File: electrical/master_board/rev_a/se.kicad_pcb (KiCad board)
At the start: 2 copper layers, 0 parts

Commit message: Inject the PCB outlines into master/center/ne/nw/se/sw PCB's.
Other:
- board outline added: 64.7 x 45 mm
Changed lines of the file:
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@@
     (uvia_drill 0.1)
   )
+  (gr_line (start 107.50 158.60) (end 107.50 179.49) (layer Edge.Cuts) (width 0.05))
+  (gr_line (start 107.50 179.49) (end 107.51 179.62) (layer Edge.Cuts) (width 0.05))
+  (gr_line (start 107.51 179.62) (end 107.52 179.76) (layer Edge.Cuts) (width 0.05))
+  (gr_line (start 107.52 179.76) (end 107.55 179.89) (layer Edge.Cuts) (width 0.05))
+  (gr_line (start 107.55 179.89) (end 107.59 180.01) (layer Edge.Cuts) (width 0.05))
+  (gr_line (start 107.59 180.01) (end 107.64 180.14) (layer Edge.Cuts) (width 0.05))
+  (gr_line (start 107.64 180.14) (end 107.71 180.25) (layer Edge.Cuts) (width 0.05))
+  (gr_line (start 107.71 180.25) (end 107.78 180.36) (layer Edge.Cuts) (width 0.05))
+  (gr_line (start 107.78 180.36) (end 107.86 180.47) (layer Edge.Cuts) (width 0.05))
+  (gr_line (start 107.86 180.47) (end 107.95 180.57) (layer Edge.Cuts) (width 0.05))
+  (gr_line (start 107.95 180.57) (end 108.05 180.65) (layer Edge.Cuts) (width 0.05))
+  (gr_line (start 108.05 180.65) (end 108.16 180.73) (layer Edge.Cuts) (width 0.05))
+  (gr_line (start 108.16 180.73) (end 108.27 180.80) (layer Edge.Cuts) (width 0.05))
+  (gr_line (start 108.27 180.80) (end 108.39 180.86) (layer Edge.Cuts) (width 0.05))
+  (gr_line (start 108.39 180.86) (end 108.51 180.91) (layer Edge.Cuts) (width 0.05))
+  (gr_line (start 108.51 180.91) (end 108.64 180.95) (layer Edge.Cuts) (width 0.05))
+  (gr_line (start 108.64 180.95) (end 108.77 180.97) (layer Edge.Cuts) (width 0.05))
+  (gr_line (start 108.77 180.97) (end 108.90 180.99) (layer Edge.Cuts) (width 0.05))
+  (gr_line (start 108.90 180.99) (end 109.04 180.99) (layer Edge.Cuts) (width 0.05))
+  (gr_line (start 109.04 180.99) (end 109.17 180.98) (layer Edge.Cuts) (width 0.05))
+  (gr_line (start 109.17 180.98) (end 109.17 180.98) (layer Edge.Cuts) (width 0.05))
+  (gr_line (start 109.17 180.98) (end 116.27 179.86) (layer Edge.Cuts) (width 0.05))
+  (gr_line (start 116.27 179.86) (end 123.24 178.12) (layer Edge.Cuts) (width 0.05))
+  (gr_line (start 123.24 178.12) (end 130.03 175.77) (layer Edge.Cuts) (width 0.05))
+  (gr_line (start 130.03 175.77) (end 136.59 172.83) (layer Edge.Cuts) (width 0.05))
+  (gr_line (start 136.59 172.83) (end 142.86 169.32) (layer Edge.Cuts) (width 0.05))
+  (gr_line (start 142.86 169.32) (end 148.80 165.28) (layer Edge.Cuts) (width 0.05))
+  (gr_line (start 148.80 165.28) (end 154.36 160.72) (layer Edge.Cuts) (width 0.05))
+  (gr_line (start 154.36 160.72) (end 159.50 155.70) (layer Edge.Cuts) (width 0.05))
+  (gr_line (start 159.50 155.70) (end 164.17 150.24) (layer Edge.Cuts) (width 0.05))
+  (gr_line (start 164.17 150.24) (end 168.35 144.40) (layer Edge.Cuts) (width 0.05))
+  (gr_line (start 168.35 144.40) (end 171.99 138.20) (layer Edge.Cuts) (width 0.05))
+  (gr_line (start 171.99 138.20) (end 172.05 138.08) (layer Edge.Cuts) (width 0.05))
+  (gr_line (start 172.05 138.08) (end 172.10 137.96) (layer Edge.Cuts) (width 0.05))
+  (gr_line (start 172.10 137.96) (end 172.13 137.83) (layer Edge.Cuts) (width 0.05))
+  (gr_line (start 172.13 137.83) (end 172.15 137.69) (layer Edge.Cuts) (width 0.05))
+  (gr_line (start 172.15 137.69) (end 172.17 137.56) (layer Edge.Cuts) (width 0.05))
+  (gr_line (start 172.17 137.56) (end 172.16 137.43) (layer Edge.Cuts) (width 0.05))
+  (gr_line (start 172.16 137.43) (end 172.15 137.29) (layer Edge.Cuts) (width 0.05))
+  (gr_line (start 172.15 137.29) (end 172.13 137.16) (layer Edge.Cuts) (width 0.05))
+  (gr_line (start 172.13 137.16) (end 172.09 137.03) (layer Edge.Cuts) (width 0.05))
+  (gr_line (start 172.09 137.03) (end 172.04 136.91) (layer Edge.Cuts) (width 0.05))
+  (gr_line (start 172.04 136.91) (end 171.99 136.79) (layer Edge.Cuts) (width 0.05))
+  (gr_line (start 171.99 136.79) (end 171.92 136.67) (layer Edge.Cuts) (width 0.05))
+  (gr_line (start 171.92 136.67) (end 171.84 136.56) (layer Edge.Cuts) (width 0.05))
+  (gr_line (start 171.84 136.56) (end 171.75 136.46) (layer Edge.Cuts) (width 0.05))
+  (gr_line (start 171.75 136.46) (end 171.65 136.37) (layer Edge.Cuts) (width 0.05))
+  (gr_line (start 171.65 136.37) (end 171.55 136.28) (layer Edge.Cuts) (width 0.05))
+  (gr_line (start 171.55 136.28) (end 171.43 136.21) (layer Edge.Cuts) (width 0.05))
+  (gr_line (start 171.43 136.21) (end 171.32 136.15) (layer Edge.Cuts) (width 0.05))
+  (gr_line (start 171.32 136.15) (end 171.19 136.10) (layer Edge.Cuts) (width 0.05))
+  (gr_line (start 171.19 136.10) (end 171.06 136.05) (layer Edge.Cuts) (width 0.05))
+  (gr_line (start 171.06 136.05) (end 170.93 136.02) (layer Edge.Cuts) (width 0.05))
+  (gr_line (start 170.93 136.02) (end 170.80 136.01) (layer Edge.Cuts) (width 0.05))
+  (gr_line (start 170.80 136.01) (end 170.67 136.00) (layer Edge.Cuts) (width 0.05))
+  (gr_line (start 170.67 136.00) (end 162.50 136.00) (layer Edge.Cuts) (width 0.05))
+  (gr_line (start 162.50 136.00) (end 162.50 140.55) (layer Edge.Cuts) (width 0.05))
+  (gr_line (start 162.50 140.55) (end 157.67 147.16) (layer Edge.Cuts) (width 0.05))
+  (gr_line (start 157.67 147.16) (end 152.15 153.20) (layer Edge.Cuts) (width 0.05))
+  (gr_line (start 152.15 153.20) (end 146.00 158.60) (layer Edge.Cuts) (width 0.05))
+  (gr_line (start 146.00 158.60) (end 107.50 158.60) (layer Edge.Cuts) (width 0.05))
 )

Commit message: Finally have everything fitting together.
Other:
- outline, holes or cut-outs redrawn
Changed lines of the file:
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@@
     (uvia_drill 0.1)
   )
-  (gr_line (start 107.5 158.6) (end 107.5 179.49) (layer Edge.Cuts) (width 0.05))
+  (gr_line (start 107.5 159.1) (end 107.5 179.49) (layer Edge.Cuts) (width 0.05))
   (gr_line (start 107.5 179.49) (end 107.51 179.62) (layer Edge.Cuts) (width 0.05))
   (gr_line (start 107.51 179.62) (end 107.52 179.76) (layer Edge.Cuts) (width 0.05))
@@
   (gr_line (start 170.67 136) (end 162.5 136) (layer Edge.Cuts) (width 0.05))
   (gr_line (start 162.5 136) (end 162.5 140.55) (layer Edge.Cuts) (width 0.05))
-  (gr_line (start 162.5 140.55) (end 157.67 147.16) (layer Edge.Cuts) (width 0.05))
-  (gr_line (start 157.67 147.16) (end 152.15 153.2) (layer Edge.Cuts) (width 0.05))
-  (gr_line (start 152.15 153.2) (end 146 158.6) (layer Edge.Cuts) (width 0.05))
-  (gr_line (start 146 158.6) (end 107.5 158.6) (layer Edge.Cuts) (width 0.05))
+  (gr_line (start 162.5 140.55) (end 157.5 147.37) (layer Edge.Cuts) (width 0.05))
+  (gr_line (start 157.5 147.37) (end 151.76 153.58) (layer Edge.Cuts) (width 0.05))
+  (gr_line (start 151.76 153.58) (end 145.36 159.1) (layer Edge.Cuts) (width 0.05))
+  (gr_line (start 145.36 159.1) (end 107.5 159.1) (layer Edge.Cuts) (width 0.05))
 )

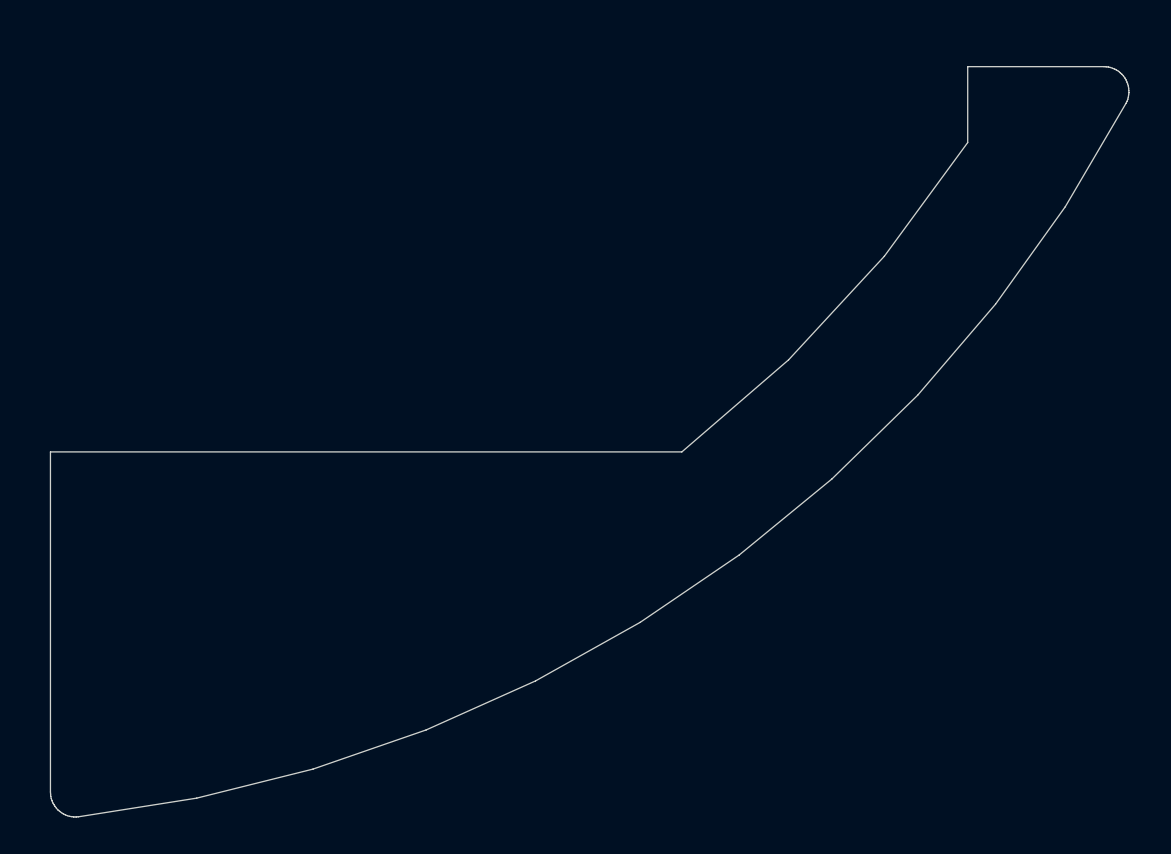
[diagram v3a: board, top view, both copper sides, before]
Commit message: Added spacer mounting holes to schematics and associated PCB's.
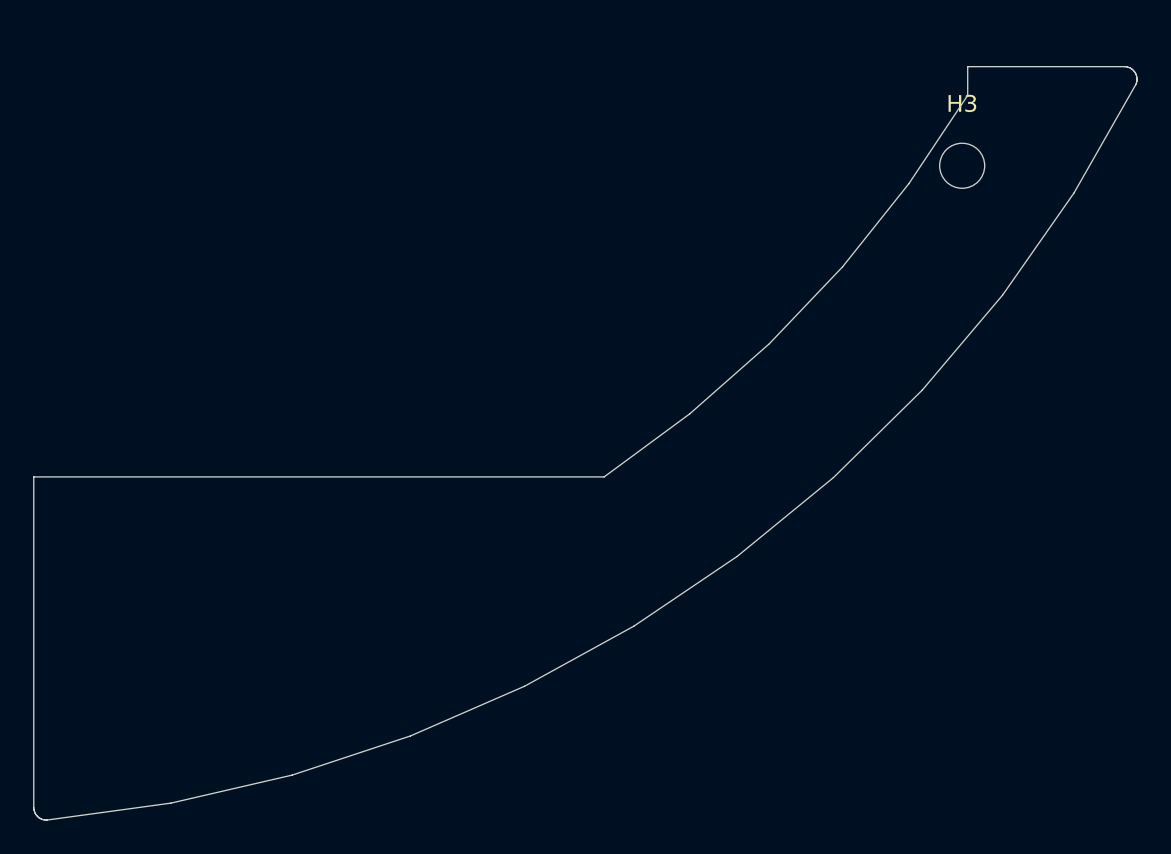
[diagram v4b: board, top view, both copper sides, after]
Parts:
- added H3: HOLE;M2.5, MountingHole:MountingHole_2.7mm_M2.5, F.Cu at (162.2, 141.9)
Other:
- board size 64.7 x 45 mm -> 66.2 x 45.2 mm

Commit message: Added LED's to the PCB's.
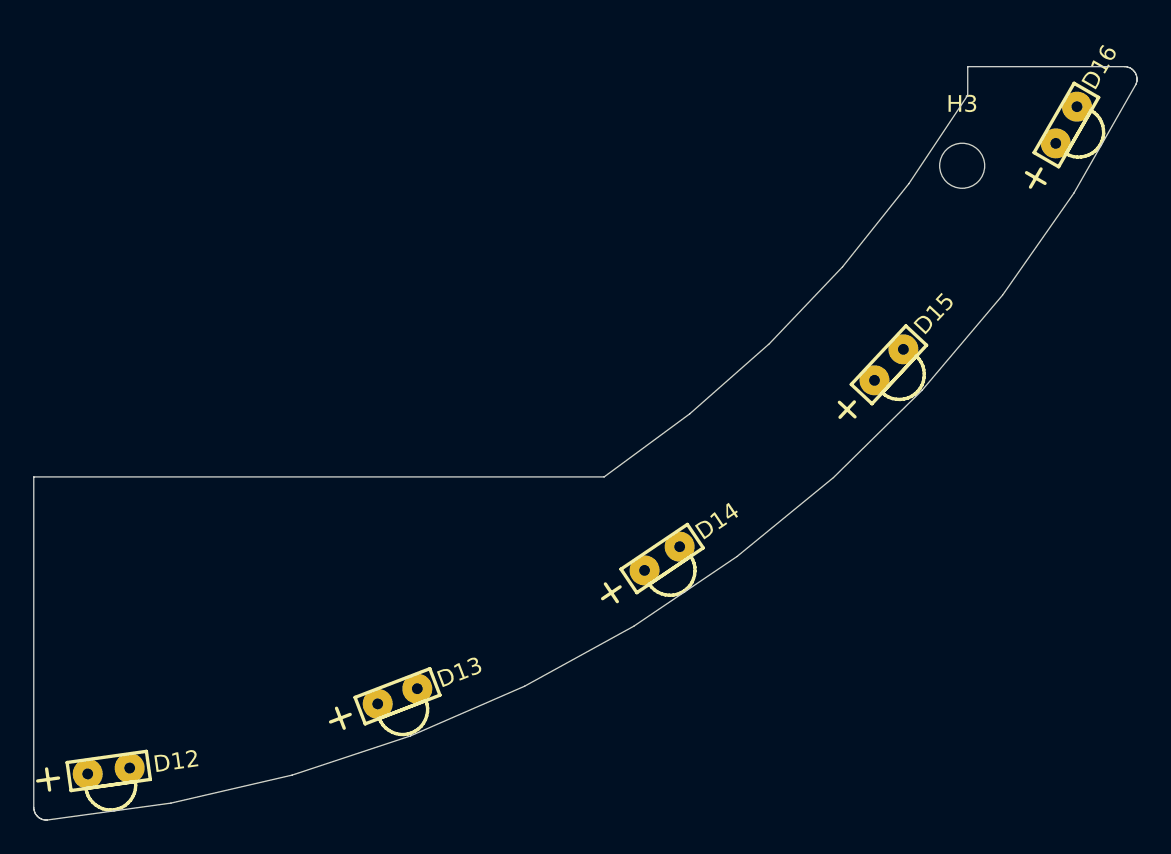
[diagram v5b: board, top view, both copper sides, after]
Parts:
- added D12: LED;GRNRA, HR2:LED_GRNRA, F.Cu at (111.0, 178.2)
- added D13: LED;GRNRA, HR2:LED_GRNRA, F.Cu at (128.3, 173.8)
- added D14: LED;GRNRA, HR2:LED_GRNRA, F.Cu at (144.2, 165.5)
- added D15: LED;GRNRA, HR2:LED_GRNRA, F.Cu at (157.8, 153.9)
- added D16: LED;GRNRA, HR2:LED_GRNRA, F.Cu at (168.4, 139.5)

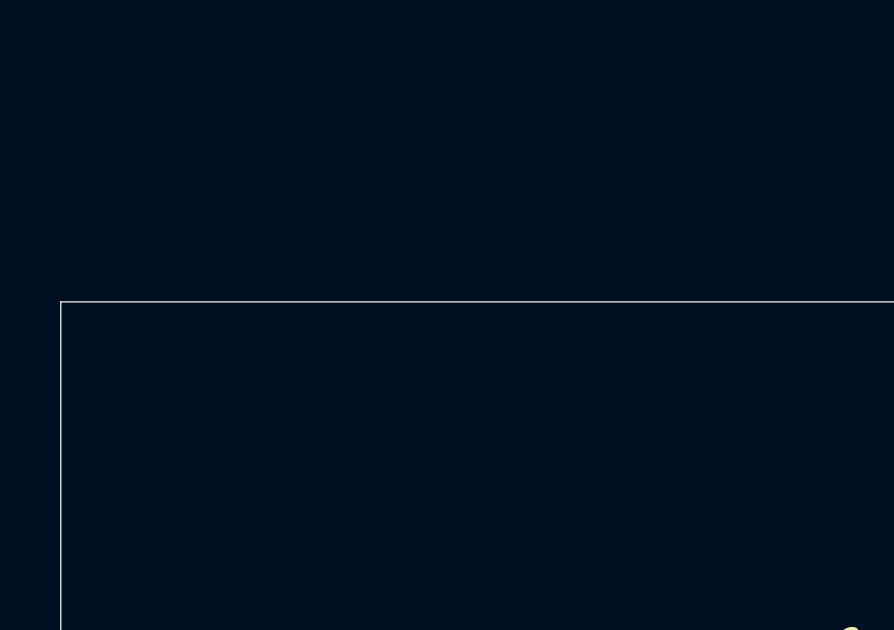
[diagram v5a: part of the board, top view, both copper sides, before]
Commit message: Got Bridge connectors installed on PCB's. Tweaking still required.
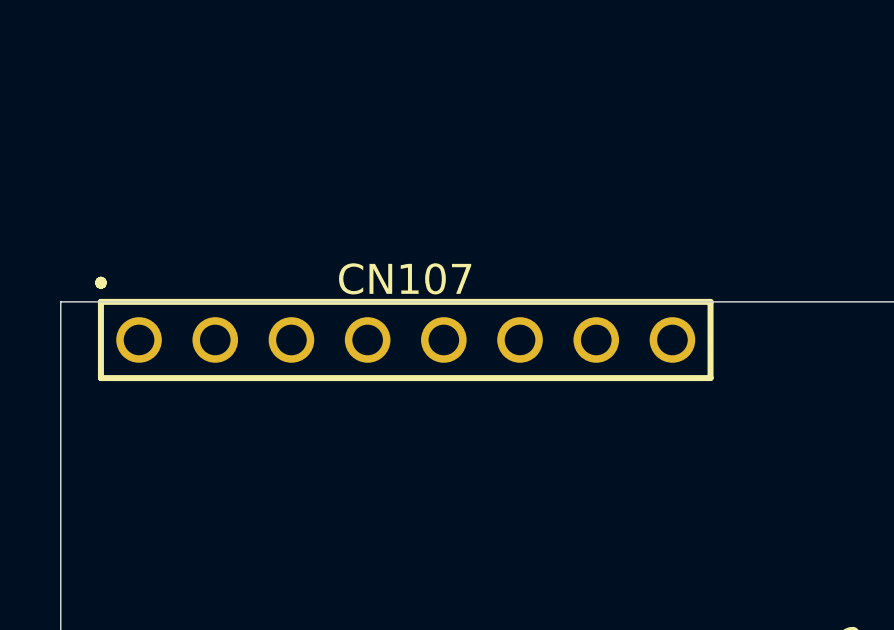
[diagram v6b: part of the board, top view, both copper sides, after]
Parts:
- added CN107: BRIDGE_SE_OUTER;M1x8, HR2:BRIDGE_SE_OUTER_M1x8, F.Cu at (118.0, 161.9)
